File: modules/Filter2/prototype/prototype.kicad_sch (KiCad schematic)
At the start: 31 parts, among them J1 Conn_01x09, U1 TL072, U2 TL074

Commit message: Filter2 prototype - wip
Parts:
- C1, C2, C3, C4: footprint (none) -> -lmp-misc:C_Rect_Kemet_L7.2mm_W2.5mm_P5mm
- C5: footprint (none) -> -lmp-misc:C_Disc_D5.0mm_W2.5mm_P2.50mm
- R1, R14, R2, R4, R7: footprint -lmp-misc:R_Axial_DIN0207_L6.3mm_D2.5mm_P7.62mm_Horizontal -> -lmp-stripboard:SB_Gen_1
- R16: footprint -lmp-misc:R_Axial_DIN0207_L6.3mm_D2.5mm_P10.16mm_Horizontal -> -lmp-stripboard:SB_Gen_2
- R5: footprint -lmp-misc:R_Axial_DIN0207_L6.3mm_D2.5mm_P7.62mm_Horizontal -> -lmp-stripboard:SB_Gen_4
- R6: footprint -lmp-misc:R_Axial_DIN0207_L6.3mm_D2.5mm_P7.62mm_Horizontal -> -lmp-stripboard:SB_Gen_7
- RV1, RV3: footprint (none) -> -lmp-synth:Potentiometer_Alpha_RD902F-40-00D_Dual_Vertical
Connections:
- net +12V: now also U1.8 (V+); no longer U1.4 (V-)
- net -12V: now also U1.4 (V-); no longer U1.8 (V+)
- net GND: now also C6.2, C7.1
- net at C1.2, R2.1: now also U1.5 (+); no longer U1.3 (+)
- net at C4.2, R14.1: now also U1.3 (+); no longer U1.5 (+)
- net at C5.1, R15.1: now also U1.2 (-); no longer U1.6 (-)
- net at C5.2, R16.1: now also U1.1; no longer U1.7
- new net: RV1.1, U1.6 (-), U1.7

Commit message: Filter2 prototype
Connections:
- net FILTER-IN: now reaches R3.1, RV1.2
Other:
- moved on the sheet: C1, R1, R2, RV1A, U1B

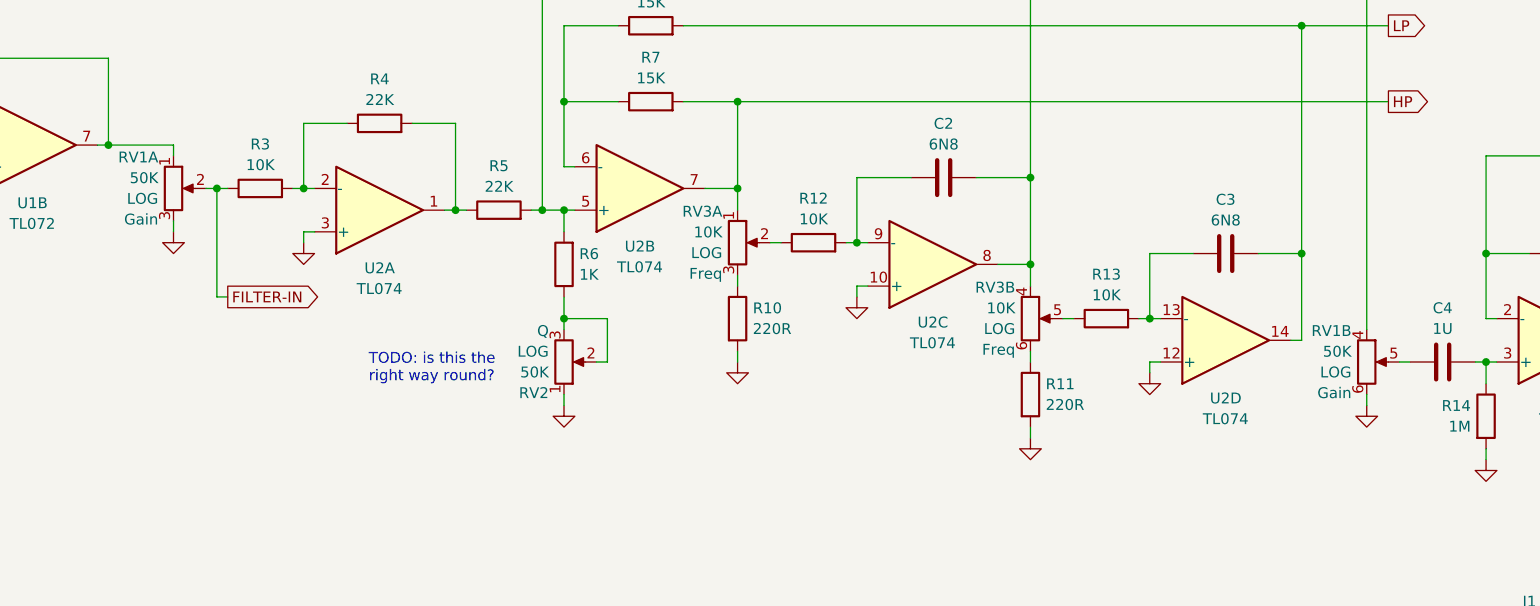
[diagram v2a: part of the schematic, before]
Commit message: Filter2 prototype & simulation
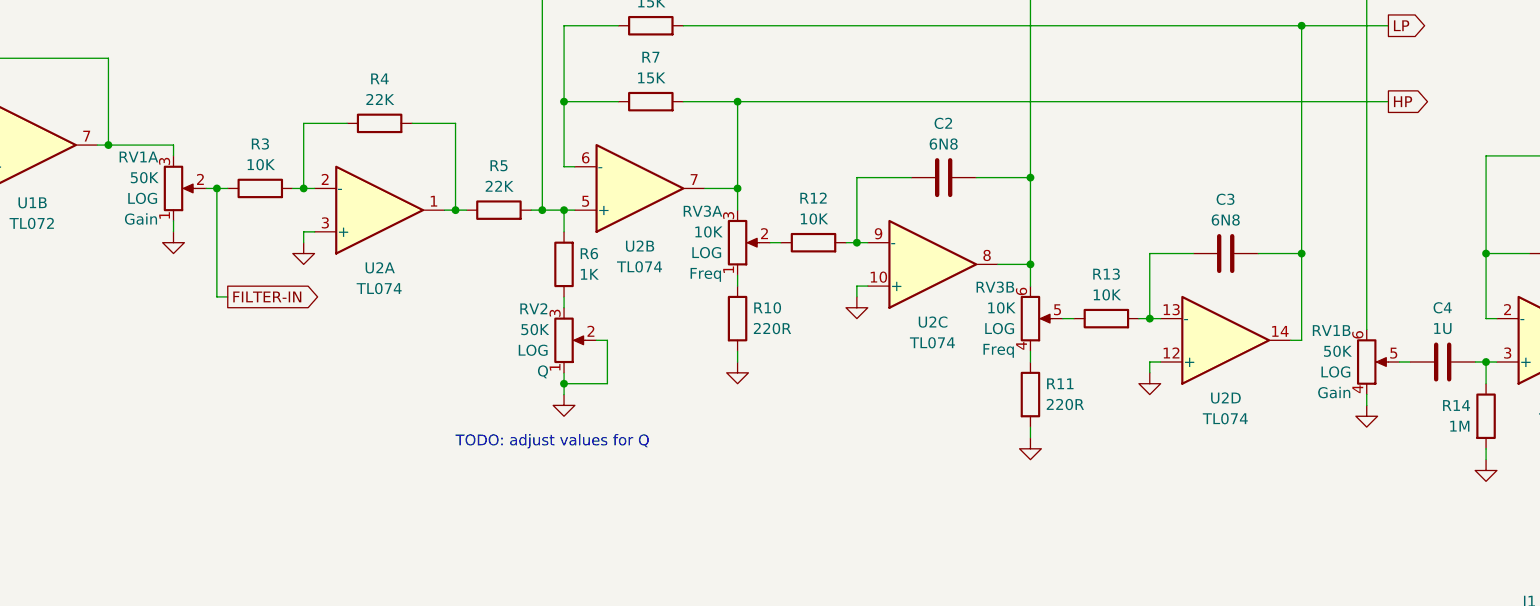
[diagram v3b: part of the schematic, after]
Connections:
- net BP: now also RV1.6, RV3.6; no longer RV1.4, RV3.4
- net GND: now also RV1.1, RV1.4, RV2.2; no longer RV1.3, RV1.6
- net HP: now also RV3.3; no longer RV3.1
- net at R11.1: now also RV3.4; no longer RV3.6
- net at U1.6 (-), U1.7: now also RV1.3; no longer RV1.1
- net at R6.1, RV2.3: no longer RV2.2
- net at R10.1: now also RV3.1; no longer RV3.3
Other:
- note added: "TODO: adjust values for Q"
- note removed: "TODO: is this the right way round?"
- moved on the sheet: RV2

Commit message: Filter2 prototype BOM
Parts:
- C2, C3: Note (none) -> sub 1U
- C5: Note (none) -> sub 18PF
- RV2: Note (none) -> sub 100K
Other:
- moved on the sheet: C1, C2, C3, C4, C5, R1, R10, R11, R12, R13, R14, R15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

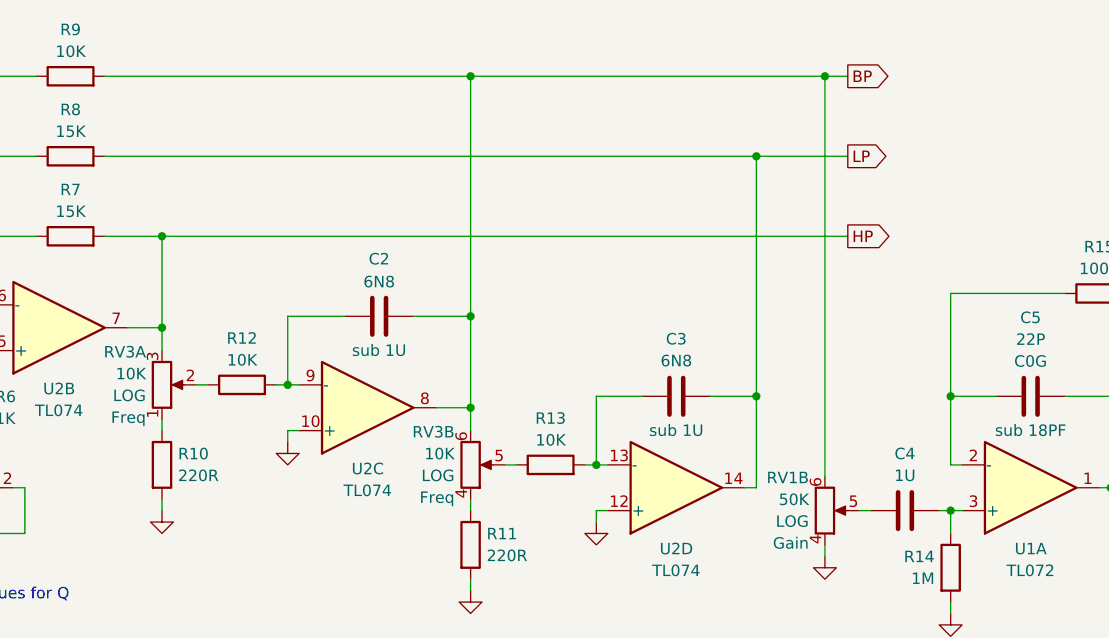
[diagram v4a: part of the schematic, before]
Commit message: Filter2 prototype - add 3-way switch
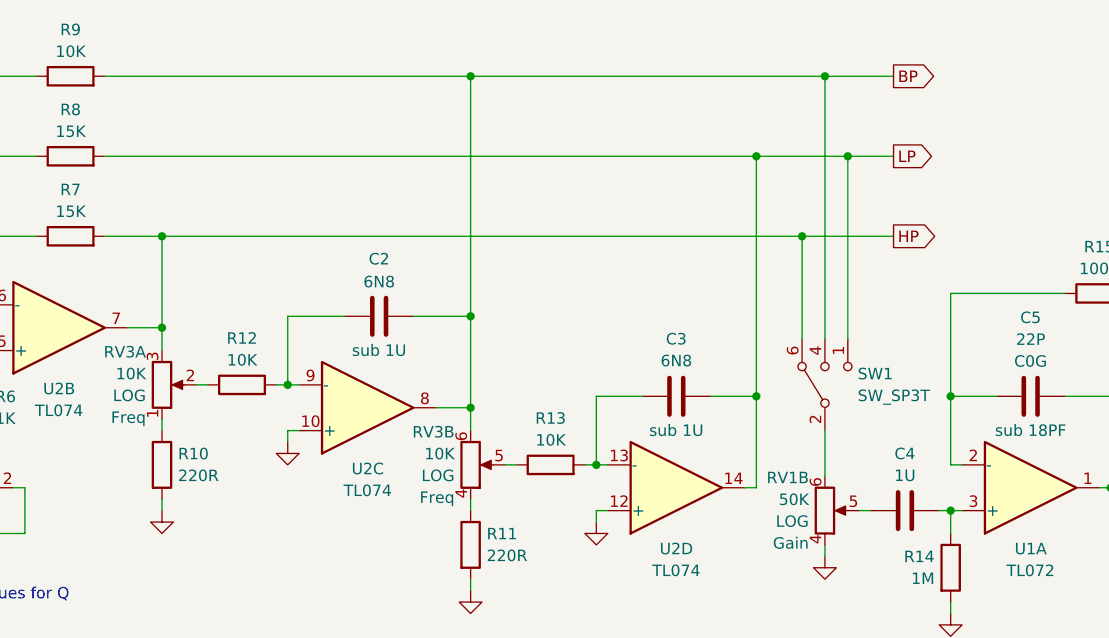
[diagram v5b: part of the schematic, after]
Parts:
- added SW1: SW_SP3T, -lmp-misc:SW_SP3T_A24JP, symbol -lmp-synth:SW_SP3T_NKK
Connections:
- net BP: now also SW1.4; no longer RV1.6
- net HP: now also SW1.6
- net LP: now also SW1.1
- new net: RV1.6, SW1.2

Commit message: Filter2 - prototype tweaks
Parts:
- C6, C7, C8, C9: now not fitted
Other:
- note added: "Who needs these caps anyway?"

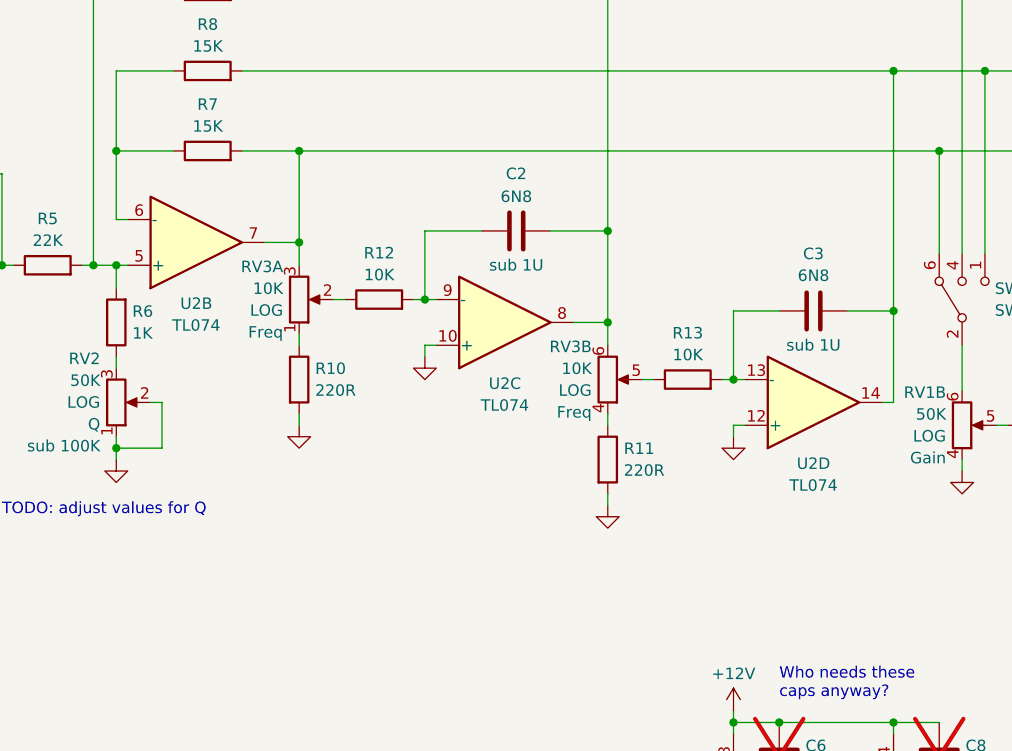
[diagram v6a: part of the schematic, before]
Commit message: Filter2 prototype - change some component values
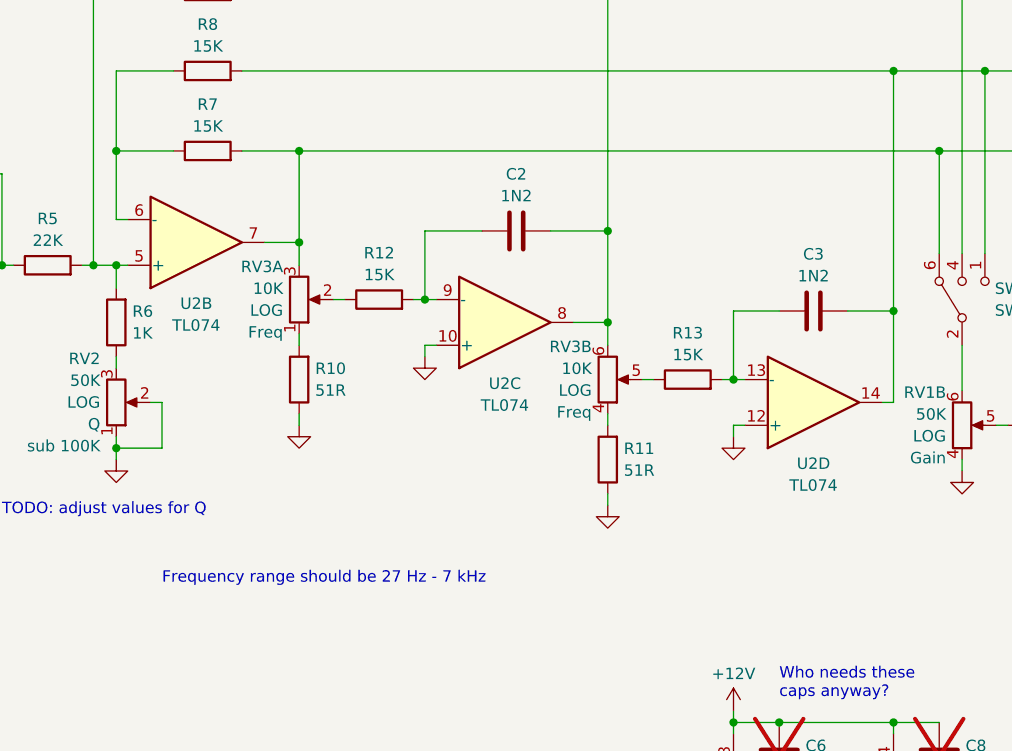
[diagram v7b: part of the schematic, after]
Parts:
- removed R10, R11: 220R, -lmp-misc:R_Axial_DIN0207_L6.3mm_D2.5mm_P7.62mm_Horizontal, symbol -lmp:R_1%_0W166
- added R10, R11: 51R, -lmp-misc:R_Axial_DIN0207_L6.3mm_D2.5mm_P7.62mm_Horizontal, symbol -lmp-synth:R_51R_Output
- C2, C3: value 6N8 -> 1N2; Note sub 1U -> (none)
- R12, R13: value 10K -> 15K
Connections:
- net GND: now also R10.1, R11.1
- net at RV3.4: now also R11.2
- net at RV3.1: now also R10.2
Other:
- note added: "Frequency range should be 27 Hz - 7 kHz"

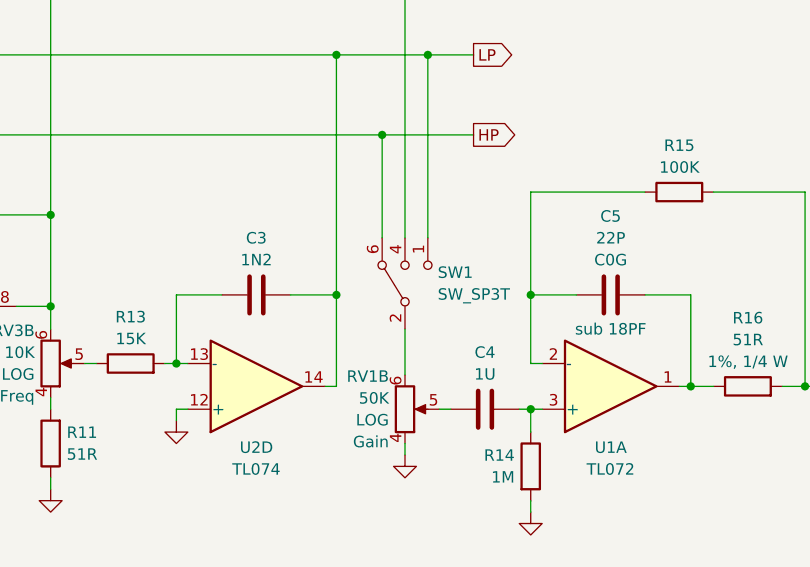
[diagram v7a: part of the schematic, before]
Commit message: Filter2 prototype - layout tweaks and remove switch
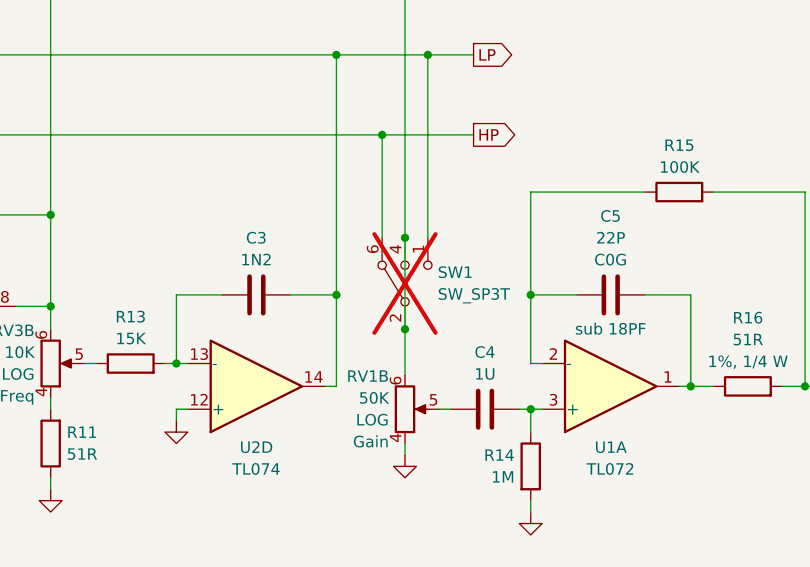
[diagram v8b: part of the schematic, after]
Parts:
- SW1: now not fitted
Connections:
- net BP: now also RV1.6, SW1.2
